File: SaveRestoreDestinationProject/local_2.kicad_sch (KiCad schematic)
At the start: 6 parts

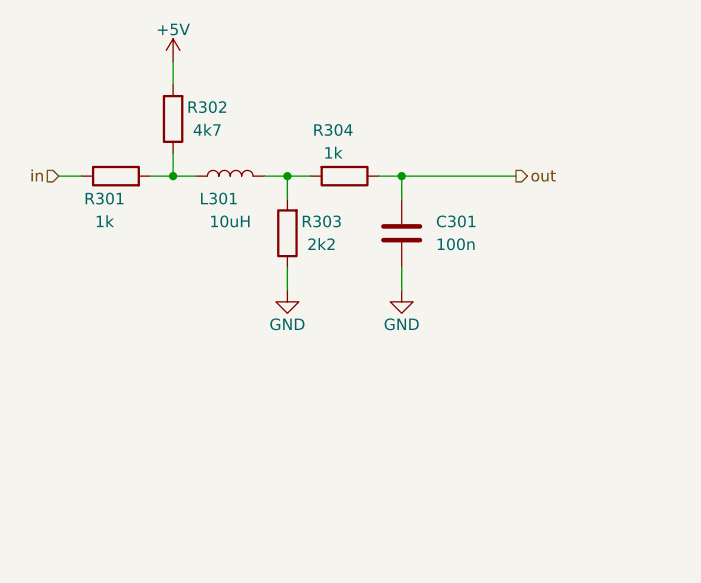
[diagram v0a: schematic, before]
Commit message: Add support for connected drawings, update test template
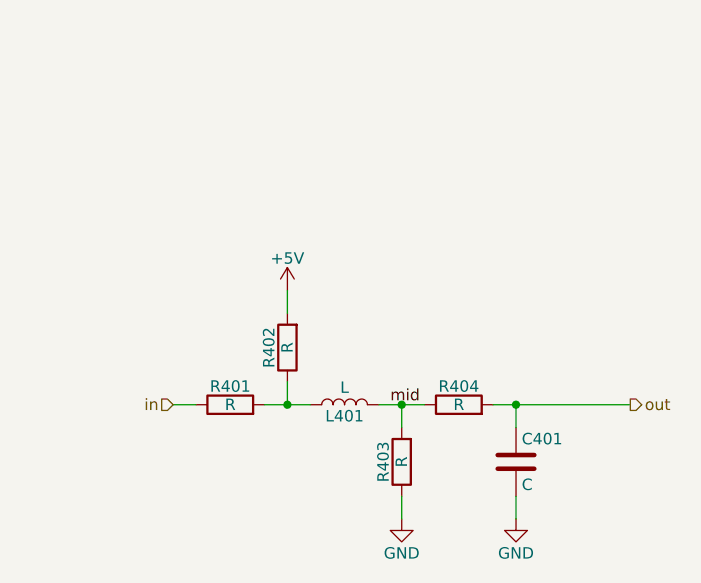
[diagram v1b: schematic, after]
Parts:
- removed C301: 100n, Capacitor_SMD:C_1206_3216Metric_Pad1.33x1.80mm_HandSolder, symbol Device:C
- removed L301: 10uH, Inductor_SMD:L_1206_3216Metric_Pad1.22x1.90mm_HandSolder, symbol Device:L
- removed R301, R304: 1k, Resistor_SMD:R_1206_3216Metric, symbol Device:R
- removed R302: 4k7, Resistor_SMD:R_1206_3216Metric, symbol Device:R
- removed R303: 2k2, Resistor_SMD:R_1206_3216Metric, symbol Device:R
- added C401: C, Capacitor_SMD:C_1206_3216Metric, symbol Device:C
- added L401: L, Inductor_SMD:L_1206_3216Metric, symbol Device:L
- added R401, R402, R403, R404: R, Resistor_SMD:R_1206_3216Metric, symbol Device:R
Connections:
- net +5V: now also R402.2
- net GND: now also C401.2, R403.1
- net in: now also R401.1
- net out: now also C401.1, R404.2
- new net: L401.1, R401.2, R402.1
- new net mid: L401.2, R403.2, R404.1
